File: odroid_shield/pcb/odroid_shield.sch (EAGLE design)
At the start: 69 parts, among them J1 AVRISP6_COMPACT, J4 ODROID_J4, U1 SINGLE-BIT_BUS_TRANSCEIVER, U10 ABM8G, U2 SINGLE-BIT_BUS_TRANSCEIVER, U3 ST1S10, U4 ATMEGA644P-20AU, U5 TS5205, U6 TCA9517MSOP8, U7 MP33926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

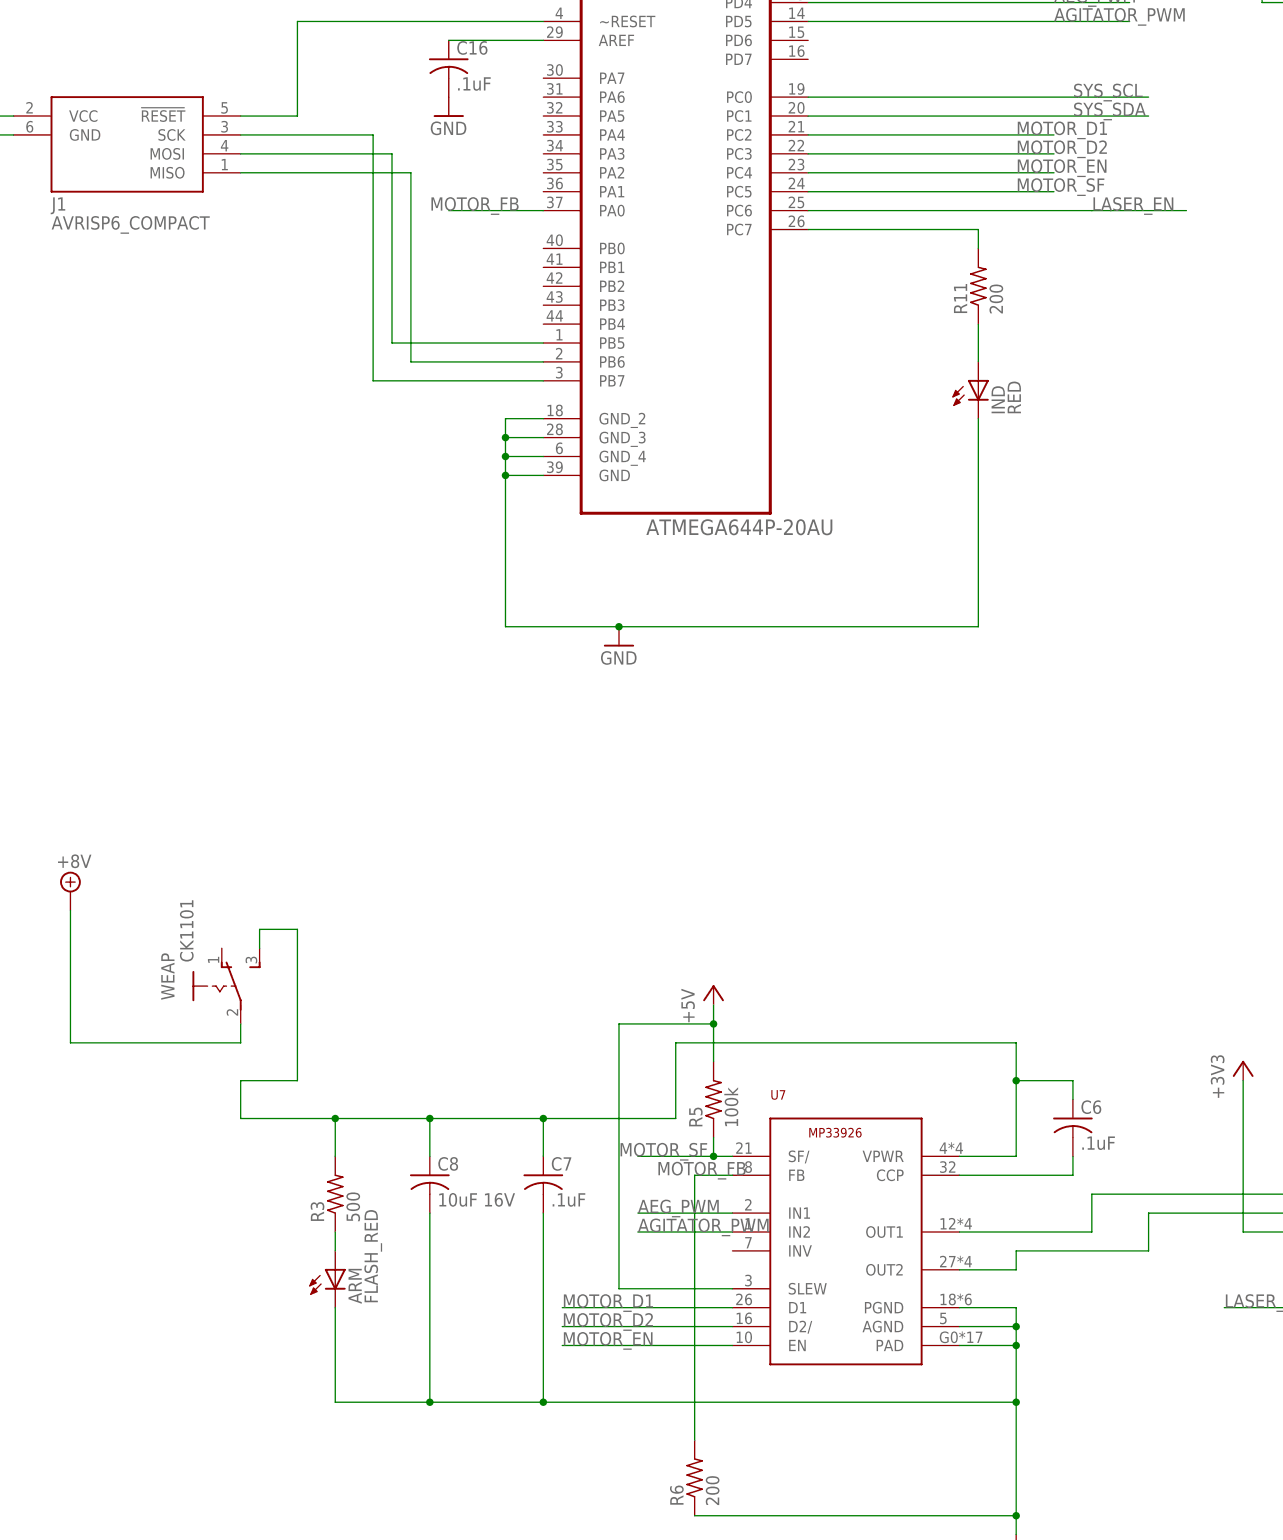
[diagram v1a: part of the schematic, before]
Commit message: odroid_shield: More progress on board.  Weapon fully routed, and I believe autoroute + some tweaks now gets a fully routable board.
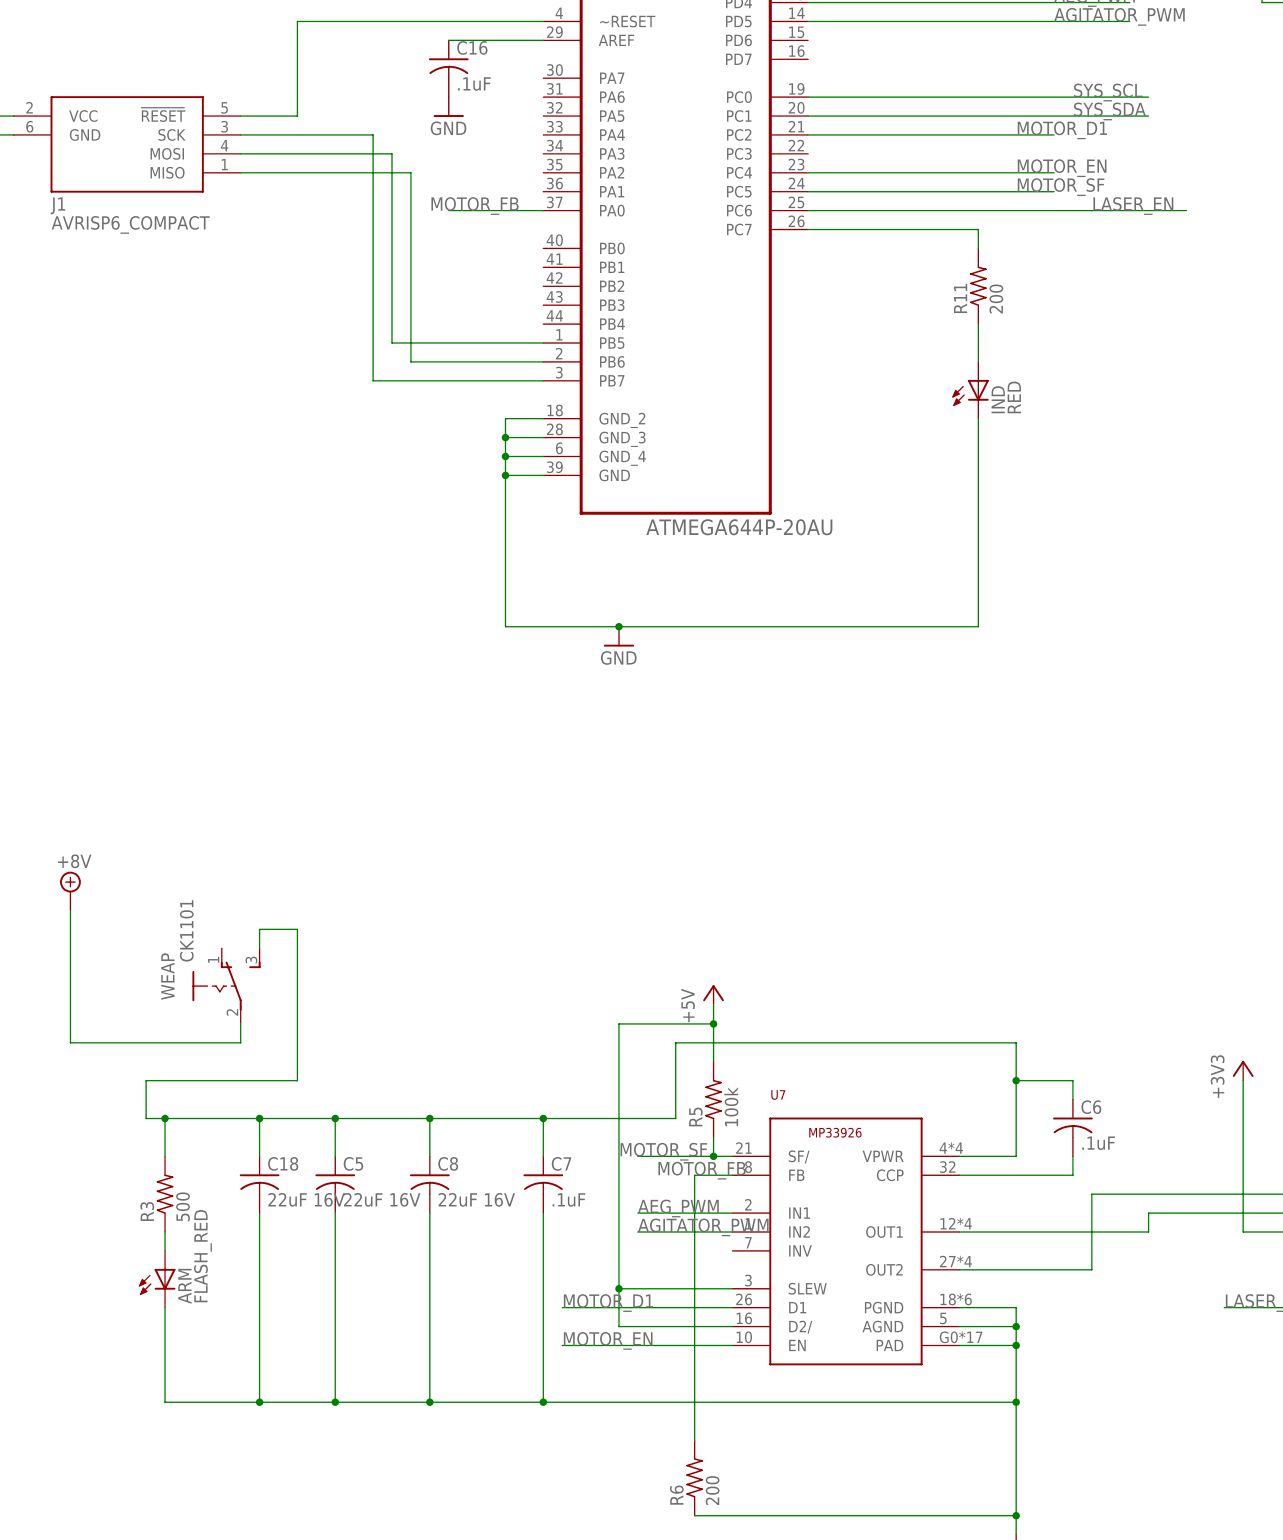
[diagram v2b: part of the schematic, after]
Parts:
- added C18, C5: 22uF 16V, rcl:C-USC1210
- C8: value 10uF 16V -> 22uF 16V; device rcl:C-USC1206 -> rcl:C-USC1210; DPN 399-7442-1-ND -> 445-3955-1-ND
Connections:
- removed net MOTOR_D2: U4.PC3, U7.D2/
- net +5V: now also U7.D2/
- net GND: now also C18.2, C5.2
- net N$12: now also U7.OUT2; no longer U7.OUT1
- net N$14: now also U7.OUT1; no longer U7.OUT2
- net N$15: now also C18.1, C5.1
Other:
- moved on the sheet: ARM, R3
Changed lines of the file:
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@@
 <part name="SUPPLY3" library="supply2" deviceset="+8V" device=""/>
 <part name="C7" library="rcl" deviceset="C-US" device="C0603" value=".1uF"/>
-<part name="C8" library="rcl" deviceset="C-US" device="C1206" value="10uF 16V">
-<attribute name="DPN" value="399-7442-1-ND"/>
+<part name="C8" library="rcl" deviceset="C-US" device="C1210" value="22uF 16V">
+<attribute name="DPN" value="445-3955-1-ND"/>
 </part>
 <part name="R3" library="rcl" deviceset="R-US_" device="R0603" value="500"/>
@@
 <part name="C17" library="rcl" deviceset="C-US" device="C0603" value=".1uF"/>
 <part name="GND18" library="supply1" deviceset="GND" device=""/>
+<part name="C5" library="rcl" deviceset="C-US" device="C1210" value="22uF 16V">
+<attribute name="DPN" value="445-3955-1-ND"/>
+</part>
+<part name="C18" library="rcl" deviceset="C-US" device="C1210" value="22uF 16V">
+<attribute name="DPN" value="445-3955-1-ND"/>
+</part>
 </parts>
 <sheets>
@@
 <instance part="B-" gate="G$1" x="66.04" y="-104.14"/>
 <instance part="GND4" gate="1" x="33.02" y="-111.76"/>
-<instance part="ARM" gate="G$1" x="40.64" y="144.78">
-<attribute name="DPN" x="40.64" y="144.78" size="1.778" layer="96" display="off"/>
+<instance part="ARM" gate="G$1" x="17.78" y="144.78">
+<attribute name="DPN" x="17.78" y="144.78" size="1.778" layer="96" display="off"/>
 </instance>
 <instance part="PWR" gate="G$1" x="53.34" y="-86.36"/>
@@
 <attribute name="DPN" x="53.34" y="157.48" size="1.778" layer="96" display="off"/>
 </instance>
-<instance part="R3" gate="G$1" x="40.64" y="154.94" rot="R90"/>
+<instance part="R3" gate="G$1" x="17.78" y="154.94" rot="R90"/>
 <instance part="R4" gate="G$1" x="53.34" y="-76.2" rot="R90"/>
 <instance part="U7" gate="G$1" x="109.22" y="149.86"/>
@@
 <instance part="C17" gate="G$1" x="50.8" y="335.28"/>
 <instance part="GND18" gate="1" x="50.8" y="327.66"/>
+<instance part="C5" gate="G$1" x="40.64" y="157.48">
+<attribute name="DPN" x="40.64" y="157.48" size="1.778" layer="96" display="off"/>
+</instance>
+<instance part="C18" gate="G$1" x="30.48" y="157.48">
+<attribute name="DPN" x="30.48" y="157.48" size="1.778" layer="96" display="off"/>
+</instance>
 </instances>
 <busses>
@@
 <wire x1="78.74" y1="177.8" x2="91.44" y2="177.8" width="0.1524" layer="91"/>
 <junction x="91.44" y="177.8"/>
+<wire x1="78.74" y1="142.24" x2="78.74" y2="137.16" width="0.1524" layer="91"/>
+<junction x="78.74" y="142.24"/>
+<pinref part="U7" gate="G$1" pin="D2/"/>
+<wire x1="78.74" y1="137.16" x2="93.98" y2="137.16" width="0.1524" layer="91"/>
 </segment>
 <segment>
@@
 <junction x="68.58" y="127"/>
 <pinref part="ARM" gate="G$1" pin="C"/>
-<wire x1="40.64" y1="139.7" x2="40.64" y2="127" width="0.1524" layer="91"/>
+<wire x1="17.78" y1="139.7" x2="17.78" y2="127" width="0.1524" layer="91"/>
+<wire x1="17.78" y1="127" x2="30.48" y2="127" width="0.1524" layer="91"/>
+<junction x="53.34" y="127"/>
+<wire x1="30.48" y1="127" x2="40.64" y2="127" width="0.1524" layer="91"/>
 <wire x1="40.64" y1="127" x2="53.34" y2="127" width="0.1524" layer="91"/>
-<junction x="53.34" y="127"/>
 <wire x1="132.08" y1="127" x2="132.08" y2="134.62" width="0.1524" layer="91"/>
 <pinref part="U7" gate="G$1" pin="PAD"/>
@@
 <wire x1="132.08" y1="139.7" x2="124.46" y2="139.7" width="0.1524" layer="91"/>
 <pinref part="R6" gate="G$1" pin="1"/>
+<junction x="132.08" y="111.76"/>
+<pinref part="C5" gate="G$1" pin="2"/>
 <wire x1="88.9" y1="111.76" x2="132.08" y2="111.76" width="0.1524" layer="91"/>
-<junction x="132.08" y="111.76"/>
+<wire x1="40.64" y1="152.4" x2="40.64" y2="127" width="0.1524" layer="91"/>
+<junction x="40.64" y="127"/>
+<pinref part="C18" gate="G$1" pin="2"/>
+<wire x1="30.48" y1="152.4" x2="30.48" y2="127" width="0.1524" layer="91"/>
+<junction x="30.48" y="127"/>
 </segment>
 <segment>
@@
 <pinref part="JWEAP" gate="A" pin="1"/>
 <wire x1="142.24" y1="154.94" x2="172.72" y2="154.94" width="0.1524" layer="91"/>
-<pinref part="U7" gate="G$1" pin="OUT1"/>
-<wire x1="124.46" y1="149.86" x2="142.24" y2="149.86" width="0.1524" layer="91"/>
-<wire x1="142.24" y1="149.86" x2="142.24" y2="154.94" width="0.1524" layer="91"/>
+<wire x1="142.24" y1="154.94" x2="142.24" y2="144.78" width="0.1524" layer="91"/>
+<pinref part="U7" gate="G$1" pin="OUT2"/>
+<wire x1="142.24" y1="144.78" x2="124.46" y2="144.78" width="0.1524" layer="91"/>
 </segment>
 </net>
 <net name="N$14" class="0">
 <segment>
-<wire x1="132.08" y1="147.32" x2="149.86" y2="147.32" width="0.1524" layer="91"/>
-<wire x1="149.86" y1="147.32" x2="149.86" y2="152.4" width="0.1524" layer="91"/>
 <pinref part="JWEAP" gate="A" pin="3"/>
 <wire x1="149.86" y1="152.4" x2="172.72" y2="152.4" width="0.1524" layer="91"/>
-<pinref part="U7" gate="G$1" pin="OUT2"/>
-<wire x1="124.46" y1="144.78" x2="132.08" y2="144.78" width="0.1524" layer="91"/>
-<wire x1="132.08" y1="144.78" x2="132.08" y2="147.32" width="0.1524" layer="91"/>
+<pinref part="U7" gate="G$1" pin="OUT1"/>
+<wire x1="124.46" y1="149.86" x2="149.86" y2="149.86" width="0.1524" layer="91"/>
+<wire x1="149.86" y1="149.86" x2="149.86" y2="152.4" width="0.1524" layer="91"/>
 </segment>
 </net>
 <net name="N$15" class="0">
 <segment>
-<wire x1="27.94" y1="165.1" x2="40.64" y2="165.1" width="0.1524" layer="91"/>
+<wire x1="15.24" y1="165.1" x2="17.78" y2="165.1" width="0.1524" layer="91"/>
 <pinref part="C8" gate="G$1" pin="1"/>
+<wire x1="17.78" y1="165.1" x2="30.48" y2="165.1" width="0.1524" layer="91"/>
+<wire x1="30.48" y1="165.1" x2="40.64" y2="165.1" width="0.1524" layer="91"/>
 <wire x1="40.64" y1="165.1" x2="53.34" y2="165.1" width="0.1524" layer="91"/>
 <wire x1="53.34" y1="165.1" x2="68.58" y2="165.1" width="0.1524" layer="91"/>
@@
 <junction x="68.58" y="165.1"/>
 <pinref part="R3" gate="G$1" pin="2"/>
-<wire x1="40.64" y1="165.1" x2="40.64" y2="160.02" width="0.1524" layer="91"/>
-<junction x="40.64" y="165.1"/>
+<wire x1="17.78" y1="165.1" x2="17.78" y2="160.02" width="0.1524" layer="91"/>
+<junction x="17.78" y="165.1"/>
 <wire x1="86.36" y1="165.1" x2="86.36" y2="175.26" width="0.1524" layer="91"/>
 <wire x1="86.36" y1="175.26" x2="132.08" y2="175.26" width="0.1524" layer="91"/>
@@
 <wire x1="139.7" y1="170.18" x2="139.7" y2="167.64" width="0.1524" layer="91"/>
 <junction x="132.08" y="170.18"/>
-<wire x1="27.94" y1="165.1" x2="27.94" y2="170.18" width="0.1524" layer="91"/>
-<wire x1="27.94" y1="170.18" x2="35.56" y2="170.18" width="0.1524" layer="91"/>
+<wire x1="15.24" y1="165.1" x2="15.24" y2="170.18" width="0.1524" layer="91"/>
+<wire x1="15.24" y1="170.18" x2="35.56" y2="170.18" width="0.1524" layer="91"/>
 <wire x1="35.56" y1="170.18" x2="35.56" y2="190.5" width="0.1524" layer="91"/>
 <pinref part="WEAP" gate="G$1" pin="S"/>
 <wire x1="35.56" y1="190.5" x2="30.48" y2="190.5" width="0.1524" layer="91"/>
 <wire x1="30.48" y1="190.5" x2="30.48" y2="187.96" width="0.1524" layer="91"/>
+<pinref part="C5" gate="G$1" pin="1"/>
+<wire x1="40.64" y1="165.1" x2="40.64" y2="160.02" width="0.1524" layer="91"/>
+<junction x="40.64" y="165.1"/>
+<pinref part="C18" gate="G$1" pin="1"/>
+<wire x1="30.48" y1="165.1" x2="30.48" y2="160.02" width="0.1524" layer="91"/>
+<junction x="30.48" y="165.1"/>
 </segment>
 </net>
@@
 <pinref part="R3" gate="G$1" pin="1"/>
 <pinref part="ARM" gate="G$1" pin="A"/>
-<wire x1="40.64" y1="149.86" x2="40.64" y2="147.32" width="0.1524" layer="91"/>
+<wire x1="17.78" y1="149.86" x2="17.78" y2="147.32" width="0.1524" layer="91"/>
 </segment>
 </net>
@@
 </segment>
 </net>
-<net name="MOTOR_D1" class="0">
-<segment>
-<pinref part="U4" gate="A" pin="PC2"/>
-<wire x1="104.14" y1="297.18" x2="137.16" y2="297.18" width="0.1524" layer="91"/>
-<label x="132.08" y="297.18" size="1.778" layer="95"/>
-</segment>
-<segment>
-<pinref part="U7" gate="G$1" pin="D1"/>
-<wire x1="93.98" y1="139.7" x2="71.12" y2="139.7" width="0.1524" layer="91"/>
-<label x="71.12" y="139.7" size="1.778" layer="95"/>
-</segment>
-</net>
-<net name="MOTOR_D2" class="0">
-<segment>
-<pinref part="U4" gate="A" pin="PC3"/>
-<wire x1="104.14" y1="294.64" x2="137.16" y2="294.64" width="0.1524" layer="91"/>
-<label x="132.08" y="294.64" size="1.778" layer="95"/>
-</segment>
-<segment>
-<pinref part="U7" gate="G$1" pin="D2/"/>
-<wire x1="93.98" y1="137.16" x2="71.12" y2="137.16" width="0.1524" layer="91"/>
-<label x="71.12" y="137.16" size="1.778" layer="95"/>
-</segment>
-</net>
 <net name="MOTOR_EN" class="0">
 <segment>
@@
 </segment>
 </net>
+<net name="MOTOR_D1" class="0">
+<segment>
+<pinref part="U7" gate="G$1" pin="D1"/>
+<wire x1="93.98" y1="139.7" x2="71.12" y2="139.7" width="0.1524" layer="91"/>
+<label x="71.12" y="139.7" size="1.778" layer="95"/>
+</segment>
+<segment>
+<pinref part="U4" gate="A" pin="PC2"/>
+<wire x1="104.14" y1="297.18" x2="137.16" y2="297.18" width="0.1524" layer="91"/>
+<label x="132.08" y="297.18" size="1.778" layer="95"/>
+</segment>
+</net>

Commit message: odroid_shield: More work on IMU.
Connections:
- net +3V3: now also U8.CS
- net GND: no longer U8.CS
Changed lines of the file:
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@@
 <pinref part="U8" gate="G$1" pin="GND"/>
 <wire x1="55.88" y1="401.32" x2="58.42" y2="401.32" width="0.1524" layer="91"/>
-<pinref part="U8" gate="G$1" pin="CS"/>
-<wire x1="86.36" y1="406.4" x2="91.44" y2="406.4" width="0.1524" layer="91"/>
-<wire x1="91.44" y1="406.4" x2="91.44" y2="383.54" width="0.1524" layer="91"/>
-<wire x1="91.44" y1="383.54" x2="73.66" y2="383.54" width="0.1524" layer="91"/>
-<junction x="73.66" y="383.54"/>
 <pinref part="C13" gate="G$1" pin="2"/>
 <wire x1="35.56" y1="406.4" x2="35.56" y2="383.54" width="0.1524" layer="91"/>
@@
 <wire x1="48.26" y1="411.48" x2="58.42" y2="411.48" width="0.1524" layer="91"/>
 <pinref part="R12" gate="G$1" pin="2"/>
-<wire x1="48.26" y1="436.88" x2="96.52" y2="436.88" width="0.1524" layer="91"/>
+<wire x1="48.26" y1="436.88" x2="91.44" y2="436.88" width="0.1524" layer="91"/>
+<wire x1="91.44" y1="436.88" x2="96.52" y2="436.88" width="0.1524" layer="91"/>
 <wire x1="96.52" y1="436.88" x2="96.52" y2="431.8" width="0.1524" layer="91"/>
 <junction x="48.26" y="436.88"/>
@@
 <wire x1="35.56" y1="414.02" x2="35.56" y2="416.56" width="0.1524" layer="91"/>
 <wire x1="35.56" y1="416.56" x2="48.26" y2="416.56" width="0.1524" layer="91"/>
-</segment>
-<segment>
+<pinref part="U8" gate="G$1" pin="CS"/>
+<wire x1="86.36" y1="406.4" x2="91.44" y2="406.4" width="0.1524" layer="91"/>
+<wire x1="91.44" y1="406.4" x2="91.44" y2="436.88" width="0.1524" layer="91"/>
+<junction x="91.44" y="436.88"/>
+</segment>
+<segment>

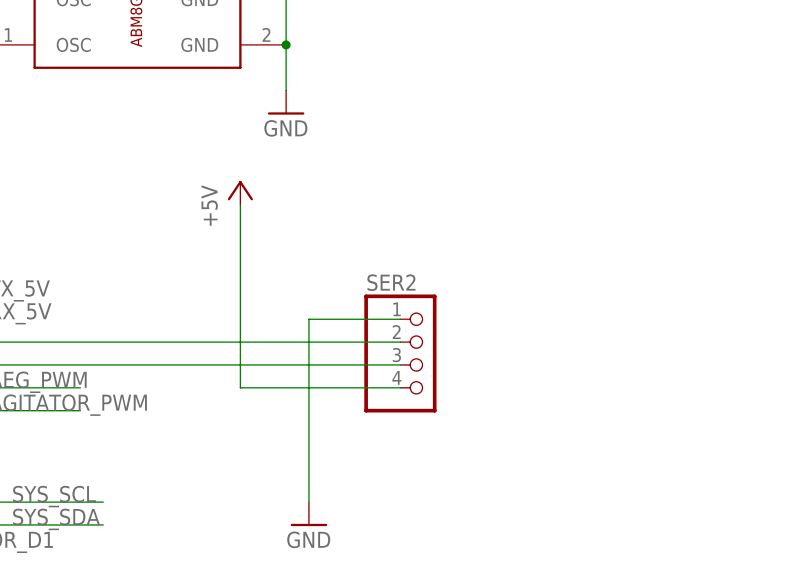
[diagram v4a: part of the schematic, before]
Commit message: odroid_shield: First pass at silk sizing and placement, pre autoroute.
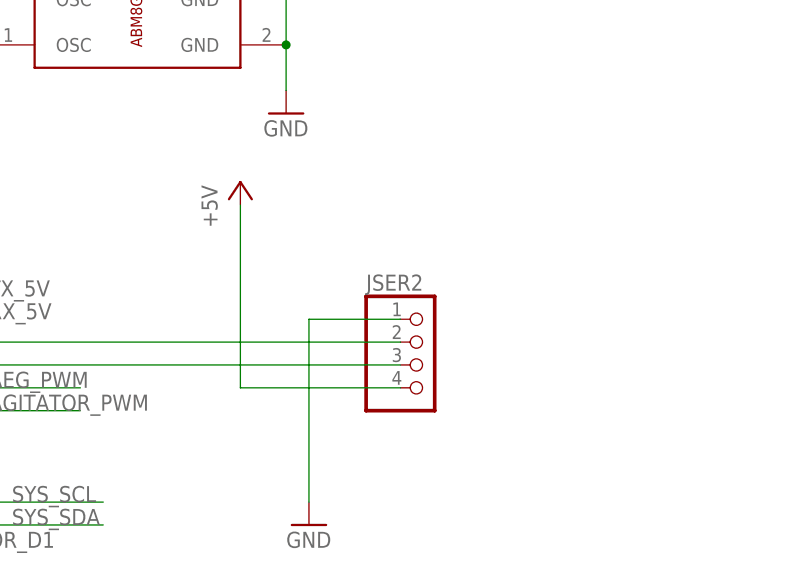
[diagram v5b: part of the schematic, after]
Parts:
- renumbered SER2 to JSER2
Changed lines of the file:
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@@
 <part name="GND11" library="supply1" deviceset="GND" device=""/>
 <part name="IND" library="led" deviceset="LED" device="CHIPLED_0805" value="RED"/>
-<part name="SER2" library="pinhead" deviceset="PINHD-1X4" device="">
+<part name="JSER2" library="pinhead" deviceset="PINHD-1X4" device="">
 <attribute name="DPN" value="S9410-ND"/>
 </part>
@@
 <instance part="GND11" gate="1" x="-7.62" y="284.48"/>
 <instance part="IND" gate="G$1" x="127" y="264.16"/>
-<instance part="SER2" gate="A" x="185.42" y="317.5">
+<instance part="JSER2" gate="A" x="185.42" y="317.5">
 <attribute name="DPN" x="185.42" y="317.5" size="1.778" layer="96" display="off"/>
 </instance>
@@
 <pinref part="P+9" gate="1" pin="+5V"/>
 <wire x1="165.1" y1="335.28" x2="165.1" y2="314.96" width="0.1524" layer="91"/>
-<pinref part="SER2" gate="A" pin="4"/>
+<pinref part="JSER2" gate="A" pin="4"/>
 <wire x1="165.1" y1="314.96" x2="182.88" y2="314.96" width="0.1524" layer="91"/>
 </segment>
@@
 <wire x1="172.72" y1="302.26" x2="172.72" y2="322.58" width="0.1524" layer="91"/>
 <wire x1="172.72" y1="322.58" x2="182.88" y2="322.58" width="0.1524" layer="91"/>
-<pinref part="SER2" gate="A" pin="1"/>
+<pinref part="JSER2" gate="A" pin="1"/>
 </segment>
 <segment>
@@
 <pinref part="U4" gate="A" pin="PD3"/>
 <wire x1="104.14" y1="317.5" x2="182.88" y2="317.5" width="0.1524" layer="91"/>
-<pinref part="SER2" gate="A" pin="3"/>
+<pinref part="JSER2" gate="A" pin="3"/>
 </segment>
 </net>
@@
 <segment>
 <pinref part="U4" gate="A" pin="PD2"/>
-<pinref part="SER2" gate="A" pin="2"/>
+<pinref part="JSER2" gate="A" pin="2"/>
 <wire x1="104.14" y1="320.04" x2="182.88" y2="320.04" width="0.1524" layer="91"/>
 </segment>
